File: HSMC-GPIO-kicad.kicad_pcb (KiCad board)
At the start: 2 copper layers, 63.5 x 78.1 mm, 114 parts, among them J1 Conn_02x20_Odd_Even, J2 HSMC_Card_QTH, J3 I2C, J4 Screw_Terminal_01x04, U1 MC78M05_TO252, U2 PCA9507

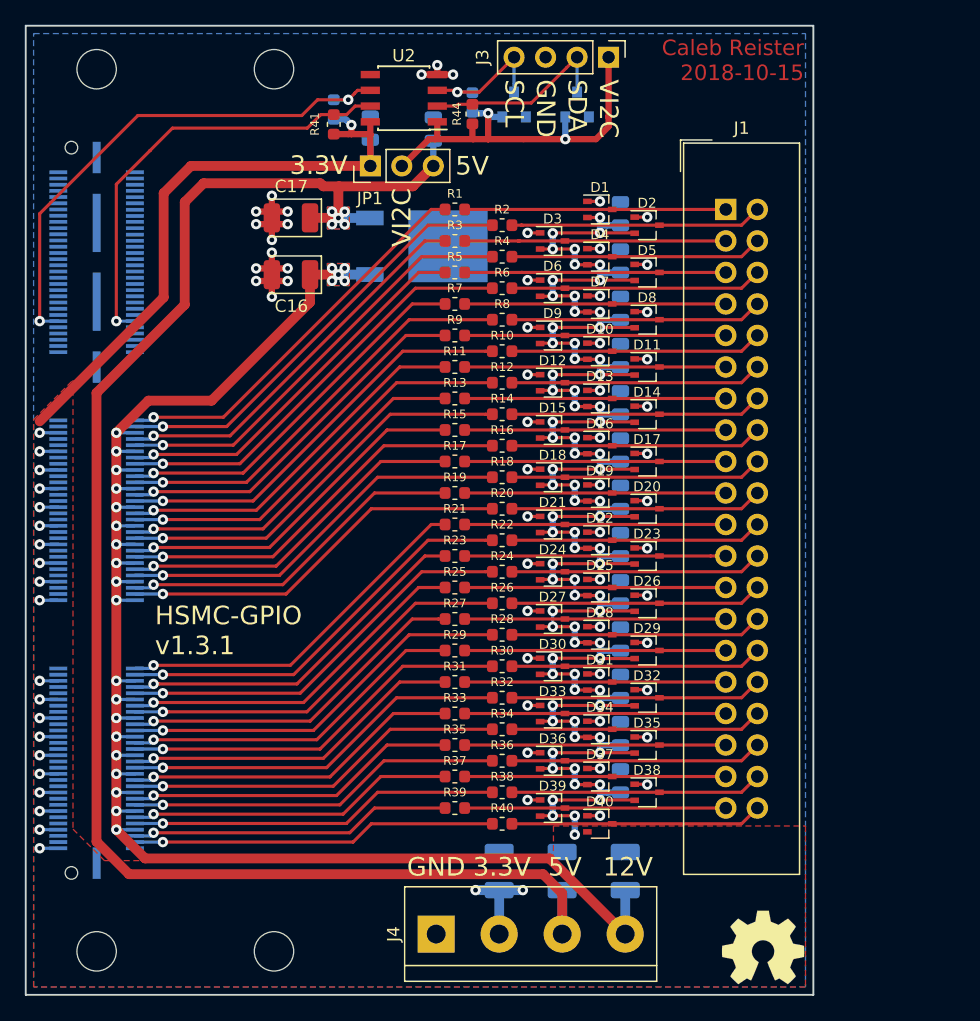
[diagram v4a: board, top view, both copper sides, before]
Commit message: Modify board to meet OSH Park specs, remove old HSMC card library.
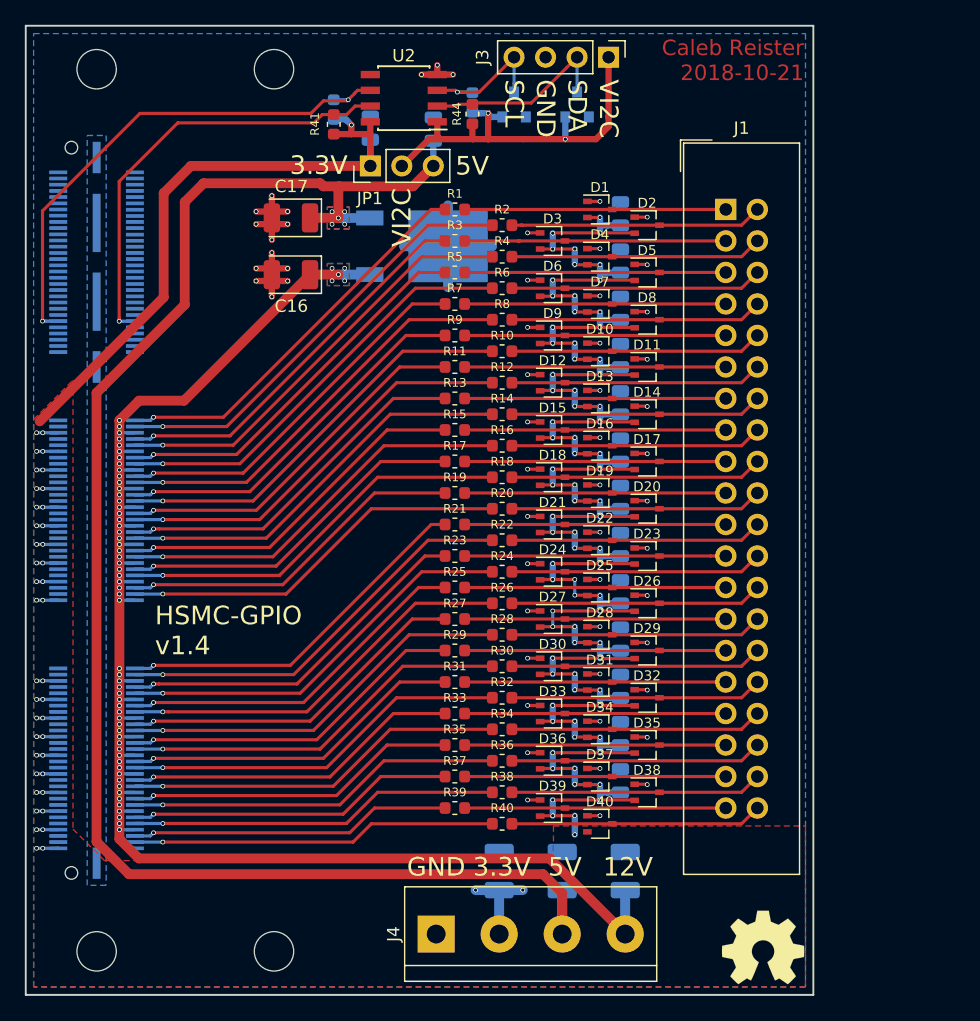
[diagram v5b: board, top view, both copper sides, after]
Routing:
- net +12V: track 136.0 -> 158.0 mm, vias 24 -> 62
- net GND: track 63.0 -> 78.3 mm
- net +3V3: track 303.5 -> 308.5 mm, vias 101 -> 121
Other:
- net class Default: via_dia 0.8382 -> 0.381; via_drill 0.381 -> 0.254
- net class Power: via_dia 0.8382 -> 0.381; via_drill 0.381 -> 0.254
- rule pad_to_mask_clearance: 0.2 -> 0.0508
- rule via_min_drill: 0.381 -> 0.254
- board text added: "Caleb Reister 2018-10-21"
- board text added: "HSMC-GPIO v1.4"
- board text removed: "Caleb Reister 2018-10-15"
- board text removed: "HSMC-GPIO v1.3.1"

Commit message: Modify power terminal
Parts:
- moved J4 0.33 mm to (58.5, 98.3)
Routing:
- net +12V: track 158.0 -> 164.1 mm
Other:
- board text added: "Caleb Reister 2018-11-12"
- board text added: "HSMC-GPIO v1.5"
- board text removed: "Caleb Reister 2018-10-21"
- board text removed: "HSMC-GPIO v1.4"
